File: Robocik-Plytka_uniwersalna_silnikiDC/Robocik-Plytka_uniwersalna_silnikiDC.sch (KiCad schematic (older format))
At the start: 66 parts, among them IC1 ACSL-6400-00TE, IC2 L6205D, J1 Conn_01x08, J2 Conn_01x02, J4 Conn_01x02, J6 Conn_01x02, Q1 BC847, Q2 BC847, Q3 BC847, U1 STM32F103C8Tx, U2 SN65HVD230, U3 LD1117S33TR_SOT223, U4 L78L05_SOT89, Y1 HSE OSC, Y2 LSE OSC

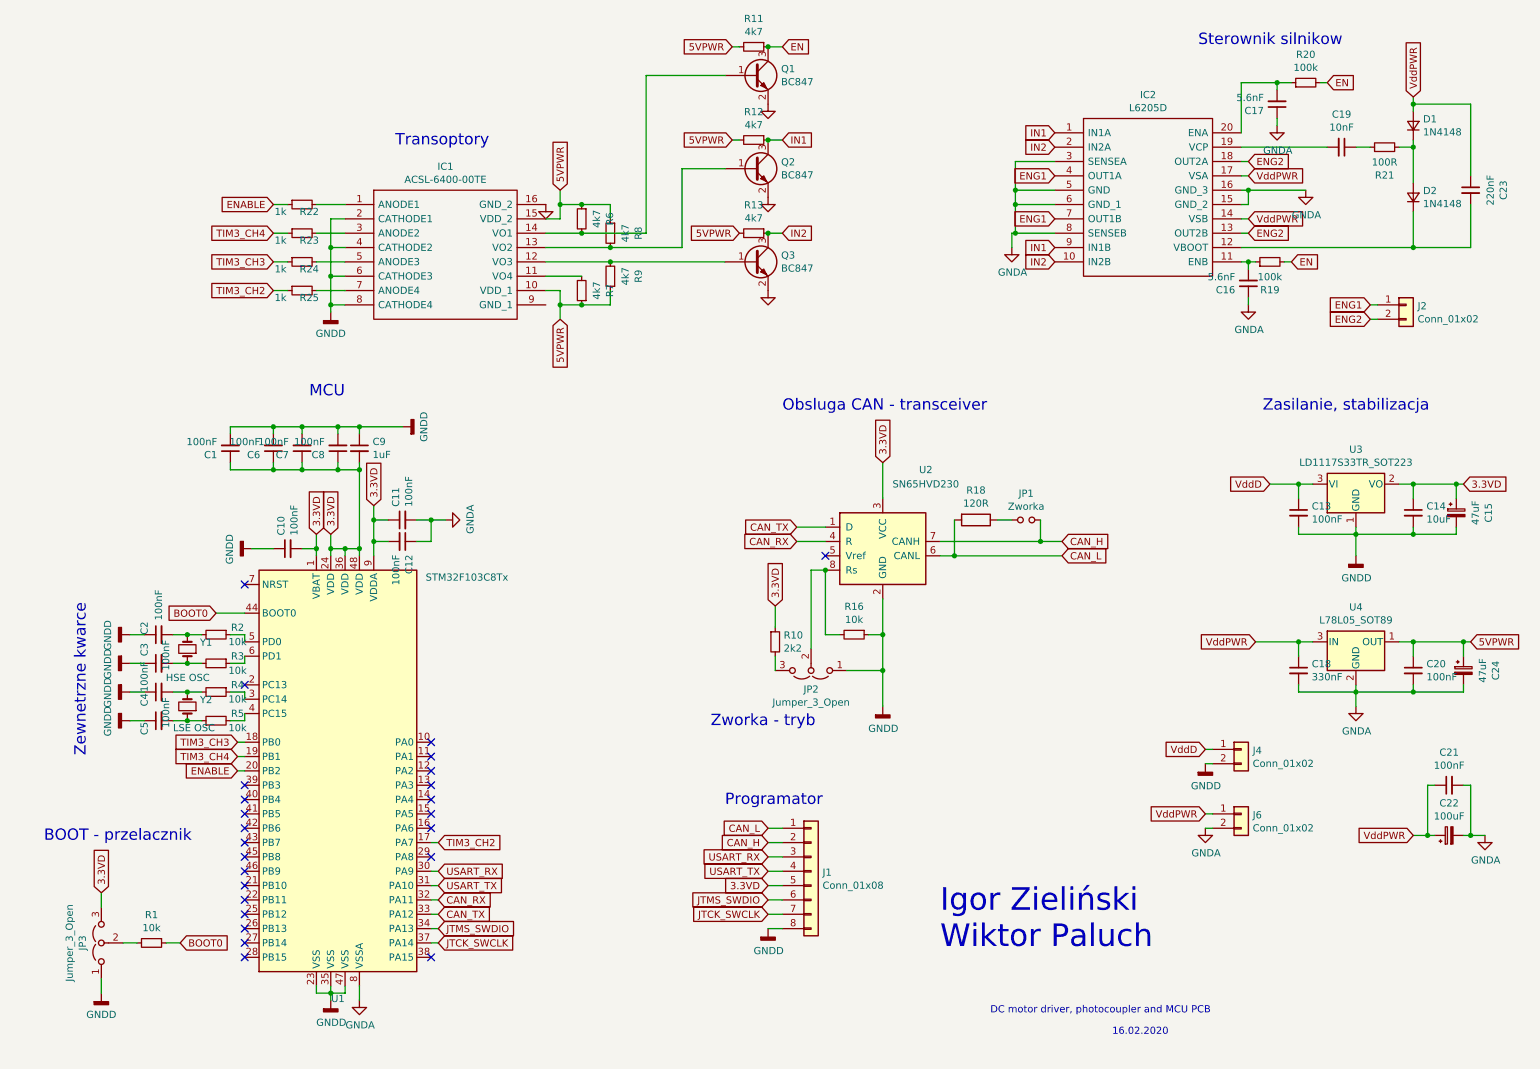
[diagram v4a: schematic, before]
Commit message: Corrected GNDA and GNDD at MCU on schematic. Changed passive elements footprints from 1206 to 0805. Corrected input capacitors placement and transoptors placement. Corrected many connections on PCB. Missing: connector footprints.
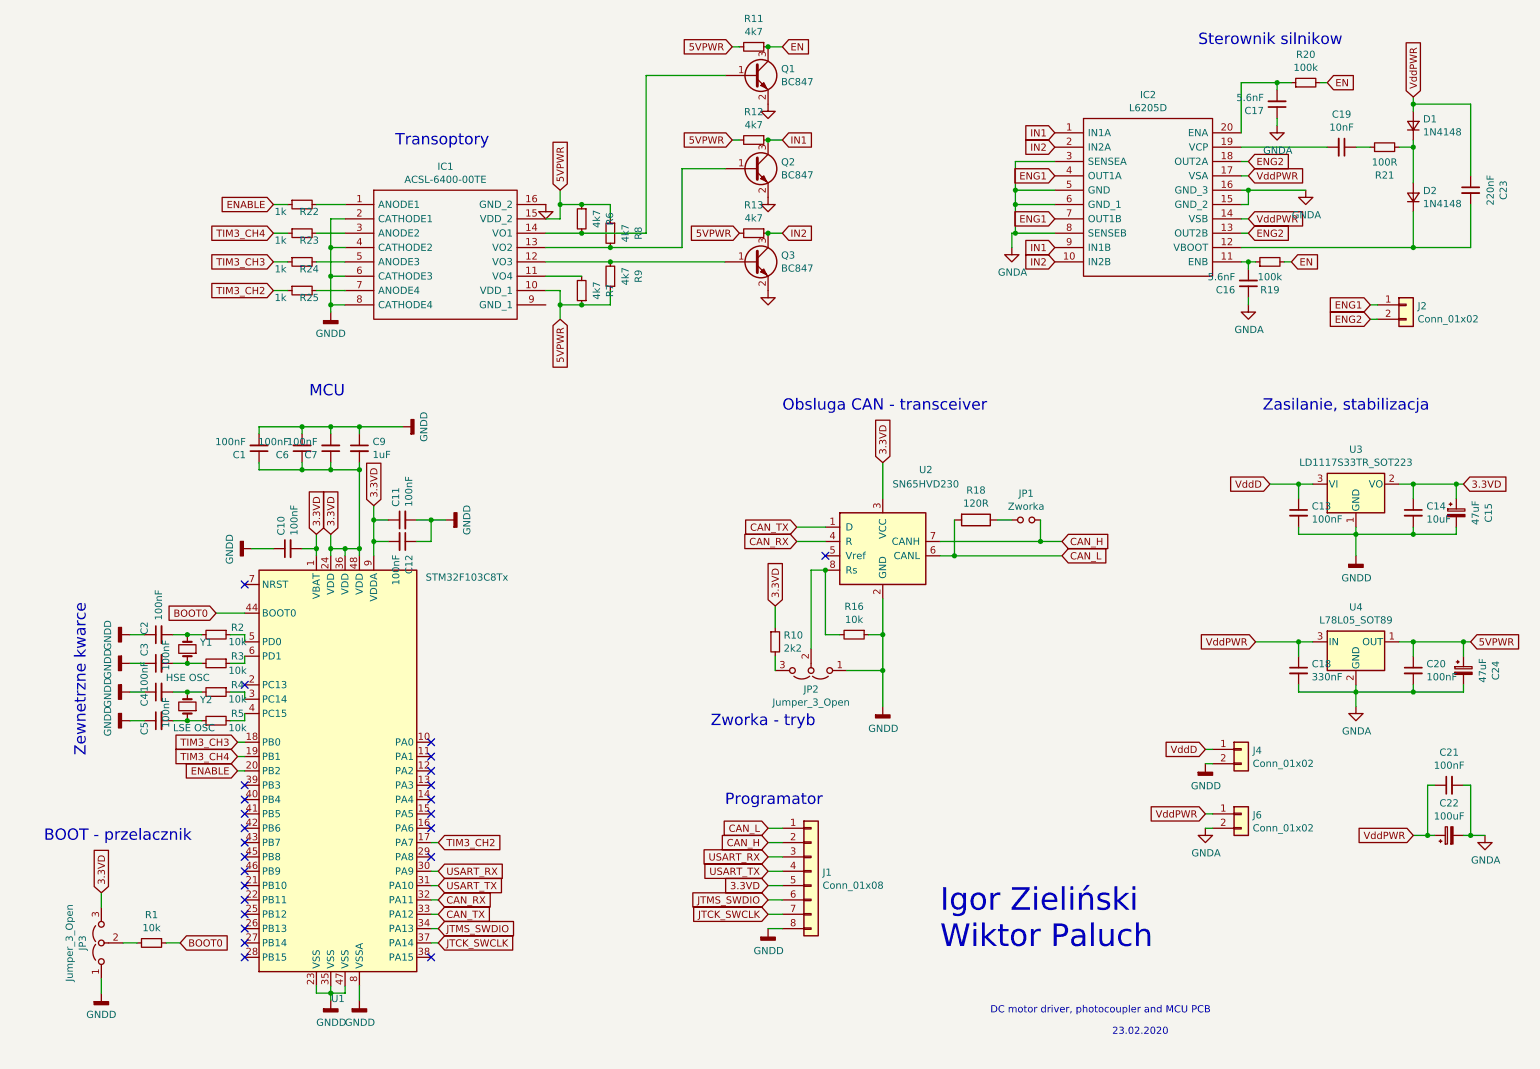
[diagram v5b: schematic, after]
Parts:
- removed C8: 100nF, Capacitor_SMD:C_1206_3216Metric, symbol Device:C_Small
- C1, C10, C11, C12, C13, C16, C17, C18, C19, C2, C20, C21, C23, C3, C4, C5, C6, C7, C9: footprint Capacitor_SMD:C_1206_3216Metric -> Capacitor_SMD:C_0805_2012Metric
- C14, C15, C24: footprint Capacitor_SMD:C_1206_3216Metric -> Capacitor_Tantalum_SMD:CP_EIA-6032-28_Kemet-C
- C22: footprint Capacitor_SMD:CP_Elec_6.3x5.8 -> Capacitor_Tantalum_SMD:CP_EIA-6032-28_Kemet-C
- R1, R10, R11, R12, R13, R16, R18, R19, R2, R20, R21, R22, R23, R24, R25, R3, R4, R5, R6, R7, R8, R9: footprint Resistor_SMD:R_1206_3216Metric -> Resistor_SMD:R_0805_2012Metric
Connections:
- net GNDA: no longer C11.2, C12.1, U1.8 (VSSA)
- net GNDD: now also C11.2, C12.1, U1.8 (VSSA)
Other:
- note added: "23.02.2020"
- note removed: "16.02.2020"
- moved on the sheet: C1, C6, C7

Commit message: Added footprints for all connectors. Moved decoupling capacitors next to engine driver. Fixed minor mistakes on PCB layout.
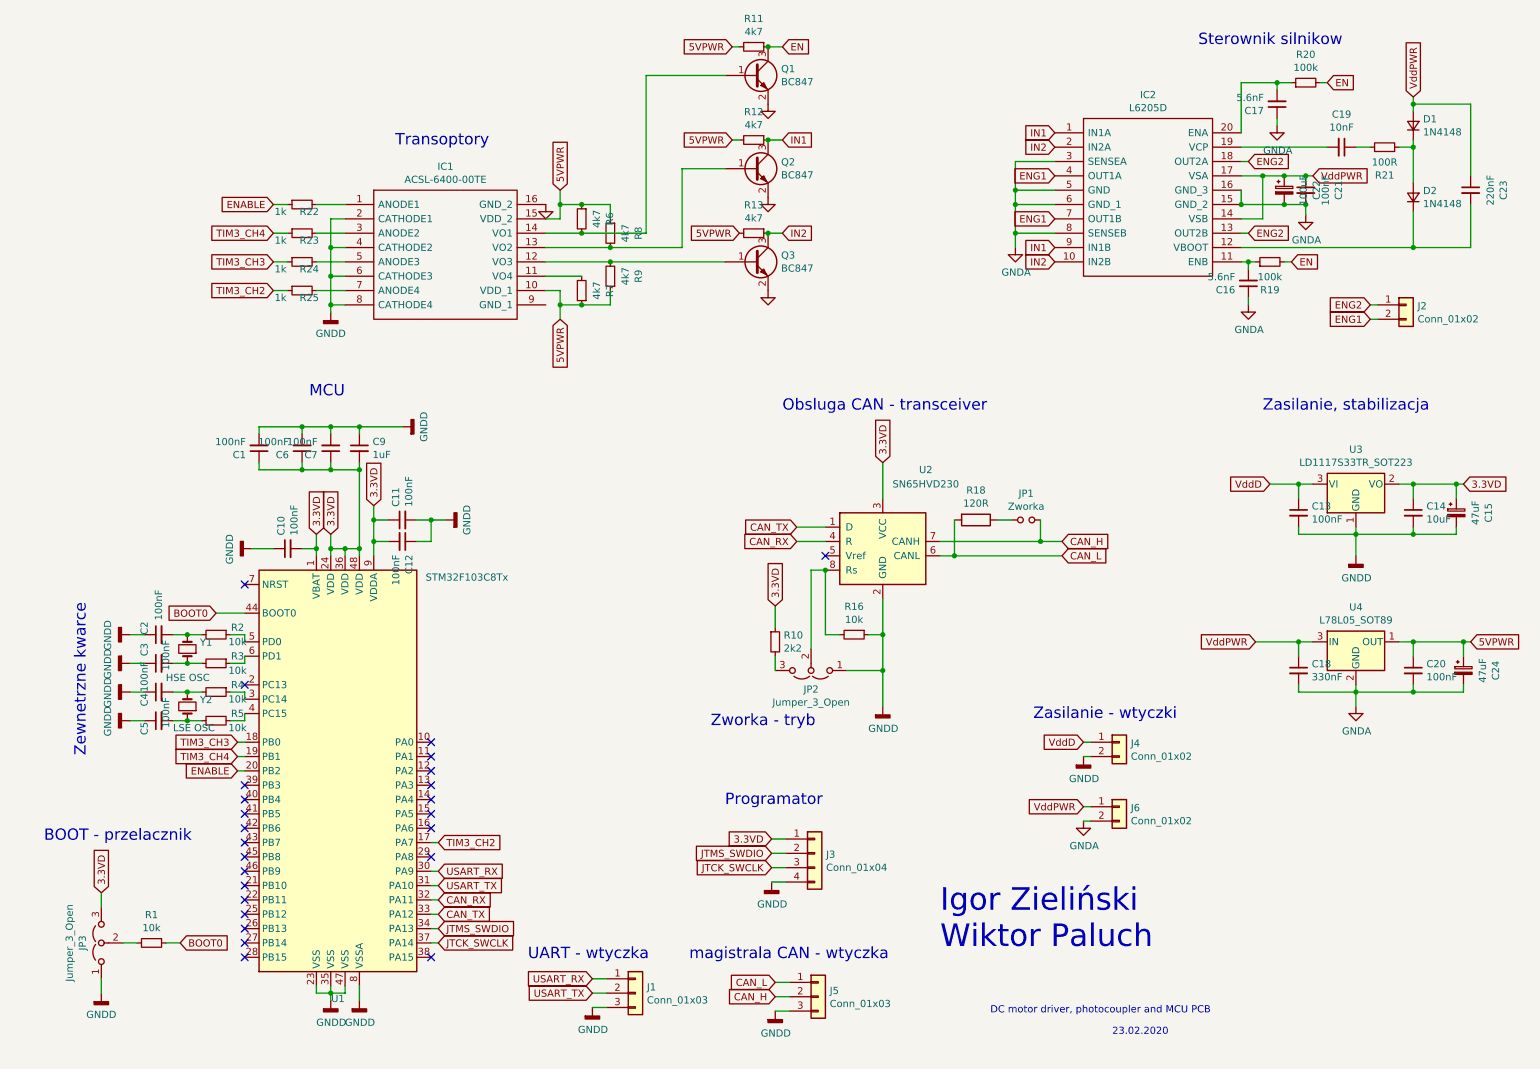
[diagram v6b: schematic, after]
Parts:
- removed J1: Conn_01x08, Connector_PinHeader_2.54mm:PinHeader_1x08_P2.54mm_Vertical, symbol Connector_Generic:Conn_01x08
- added J1: Conn_01x03, 22-05-7035:SHDR3W70P0X250_1X3_990X790X510P, symbol Connector_Generic:Conn_01x03
- added J3: Conn_01x04, 22-05-7045:22-05-7045, symbol Connector_Generic:Conn_01x04
- added J5: Conn_01x03, Connector_JST:JST_PH_S3B-PH-K_1x03_P2.00mm_Horizontal, symbol Connector_Generic:Conn_01x03
- J2: footprint Connector_PinHeader_2.54mm:PinHeader_1x02_P2.54mm_Vertical -> Connector_Molex:Molex_Mini-Fit_Jr_5569-02A2_2x01_P4.20mm_Horizontal
- J4: footprint Connector_PinHeader_2.54mm:PinHeader_1x02_P2.54mm_Vertical -> 43650-0212:43650-0214
- J6: footprint Connector_PinHeader_2.54mm:PinHeader_1x02_P2.54mm_Vertical -> Connector_Molex:Molex_Mini-Fit_Jr_5569-04A1_2x02_P4.20mm_Horizontal
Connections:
- net 3.3VD: now also J3.1 (Pin_1)
- net CAN_H: now also J5.2 (Pin_2)
- net CAN_L: now also J5.1 (Pin_1)
- net ENG1: now also J2.2 (Pin_2); no longer J2.1 (Pin_1)
- net ENG2: now also J2.1 (Pin_1); no longer J2.2 (Pin_2)
- net GNDD: now also J1.3 (Pin_3), J3.4 (Pin_4), J5.3 (Pin_3)
- net JTCK_SWCLK: now also J3.3 (Pin_3)
- net JTMS_SWDIO: now also J3.2 (Pin_2)
- net USART_RX: now also J1.1 (Pin_1)
- net USART_TX: now also J1.2 (Pin_2)
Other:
- note added: "UART - wtyczka"
- note added: "Zasilanie - wtyczki"
- note added: "magistrala CAN - wtyczka\n"
- moved on the sheet: C21, C22, J4, J6

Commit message: Changed placements of elements, added GNDA vias, updated elements designations on PCB (not finished)
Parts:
- C22: footprint Capacitor_Tantalum_SMD:CP_EIA-6032-28_Kemet-C -> Capacitor_SMD:CP_Elec_8x5.4
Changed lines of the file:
@@
 EESchema Schematic File Version 4
-LIBS:Robocik-Plytka_uniwersalna_silnikiDC-cache
-EELAYER 29 0
+EELAYER 30 0
 EELAYER END
 $Descr A4 11693 8268
@@
 F 0 "C22" V 9725 1750 50  0000 C CNN
 F 1 "100uF" V 9634 1750 50  0000 C CNN
-F 2 "Capacitor_Tantalum_SMD:CP_EIA-6032-28_Kemet-C" H 9500 1750 50  0001 C CNN
+F 2 "Capacitor_SMD:CP_Elec_8x5.4" H 9500 1750 50  0001 C CNN
 F 3 "~" H 9500 1750 50  0001 C CNN
 	1    9500 1750

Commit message: Added 3D model to all connectors, fixed some connections on PCB. Added ground layers for both GNDA and GNDD.
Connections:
- net 3.3VD: now also J3.4 (Pin_4); no longer J3.1 (Pin_1)
- net CAN_L: now also J5.3 (Pin_3); no longer J5.1 (Pin_1)
- net GNDD: now also J1.1 (Pin_1), J3.1 (Pin_1), J5.1 (Pin_1); no longer J1.3 (Pin_3), J3.4 (Pin_4), J5.3 (Pin_3)
- net JTCK_SWCLK: now also J3.2 (Pin_2); no longer J3.3 (Pin_3)
- net JTMS_SWDIO: now also J3.3 (Pin_3); no longer J3.2 (Pin_2)
- net USART_RX: now also J1.3 (Pin_3); no longer J1.1 (Pin_1)
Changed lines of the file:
@@
 EESchema Schematic File Version 4
-EELAYER 30 0
+LIBS:Robocik-Plytka_uniwersalna_silnikiDC-cache
+EELAYER 29 0
 EELAYER END
 $Descr A4 11693 8268
@@
 L Connector_Generic:Conn_01x04 J3
 U 1 1 5E5A9771
-P 6225 6375
-F 0 "J3" H 6305 6367 50  0000 L CNN
-F 1 "Conn_01x04" H 6305 6276 50  0000 L CNN
-F 2 "22-05-7045:22-05-7045" H 6225 6375 50  0001 C CNN
-F 3 "~" H 6225 6375 50  0001 C CNN
-	1    6225 6375
-	1    0    0    -1
+P 6225 6475
+F 0 "J3" H 6305 6467 50  0000 L CNN
+F 1 "Conn_01x04" H 6305 6376 50  0000 L CNN
+F 2 "22-05-7045:22-05-7045" H 6225 6475 50  0001 C CNN
+F 3 "~" H 6225 6475 50  0001 C CNN
+	1    6225 6475
+	1    0    0    1
 $EndComp
 $Comp
@@
 F 3 "~" H 6250 7375 50  0001 C CNN
 	1    6250 7375
-	1    0    0    -1
+	1    0    0    1
 $EndComp
 $Comp
@@
 F 3 "~" H 4975 7350 50  0001 C CNN
 	1    4975 7350
-	1    0    0    -1
-$EndComp
-Wire Wire Line
+	1    0    0    1
+$EndComp
+Wire Wire Line
